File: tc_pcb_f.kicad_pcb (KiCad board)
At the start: 2 copper layers, 70 x 120 mm, 7 parts, among them U1 32u4, U2 MAX31855, U3 MAX31855, U4 MAX31855, U5 MAX31855, U6 MAX31855, U7 extPWR

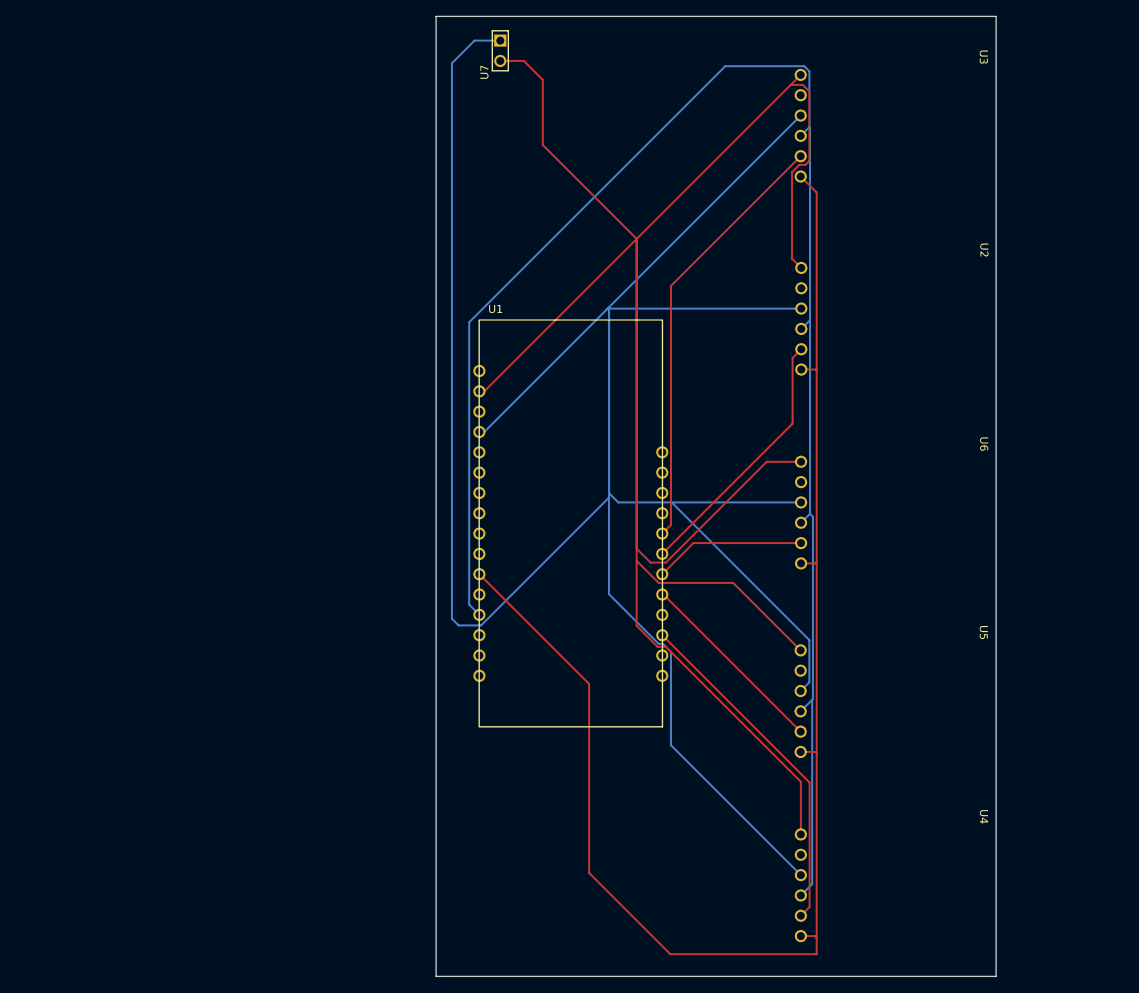
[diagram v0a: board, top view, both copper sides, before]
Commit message: finished layout for 8 sensor board
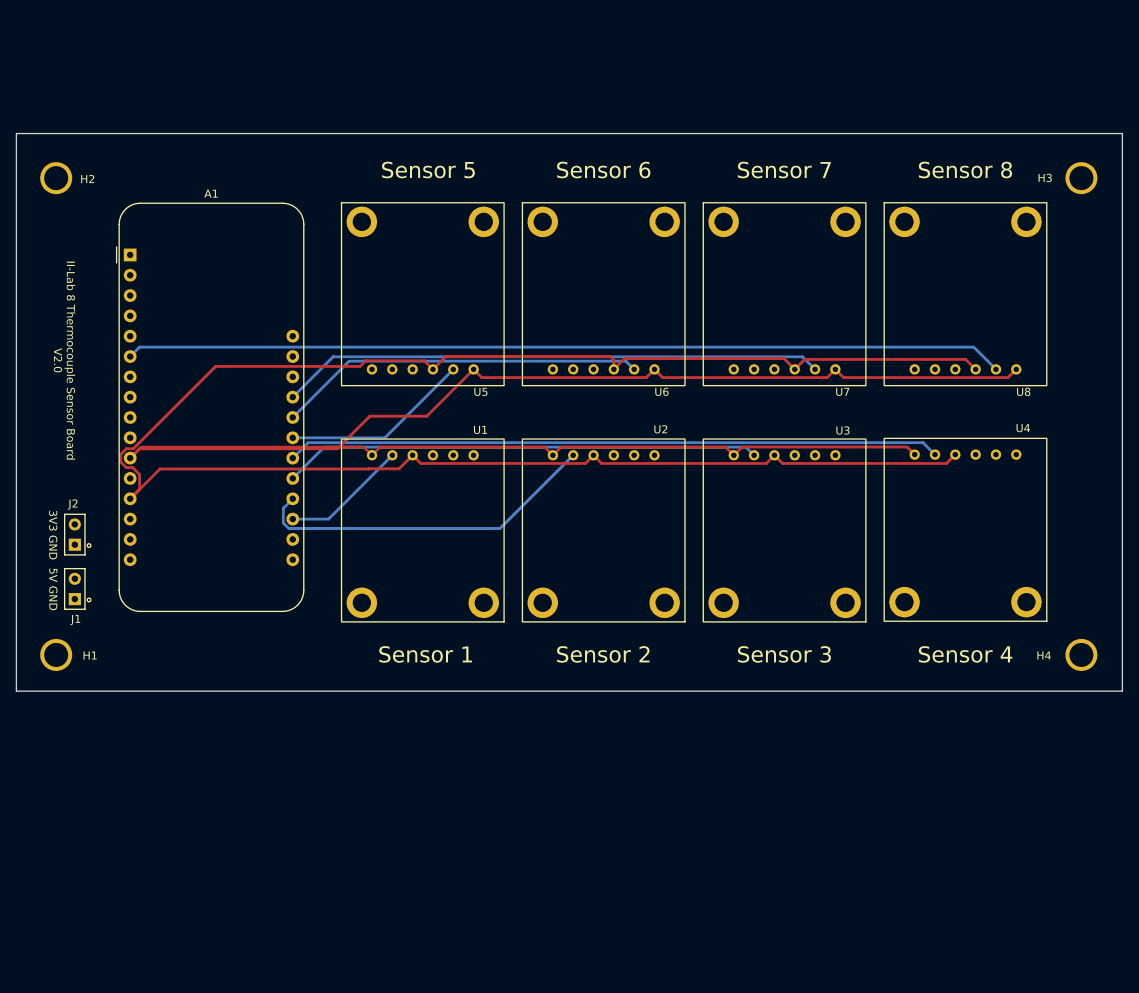
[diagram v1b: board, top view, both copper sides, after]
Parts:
- added A1: Adafruit_Feather_Generic, mcu:Adafruit_Feather, F.Cu at (61.8, 69.8)
- added H1: Conn_01x01, mounting_holes:3mm_hole, F.Cu at (58.9, 117.3)
- added H2: Conn_01x01, mounting_holes:3mm_hole, F.Cu at (52.9, 57.7)
- added H3: Conn_01x01, mounting_holes:3mm_hole, F.Cu at (181.1, 57.6)
- added H4: Conn_01x01, mounting_holes:3mm_hole, F.Cu at (69.0, 117.2)
- added J1: 5V Vin, dupont_connectors:dupont2x1, F.Cu at (52.3, 110.3)
- added J2: 3V3 Vin, dupont_connectors:dupont2x1, F.Cu at (52.3, 103.5)
- added U8: MAX31855, max:adafruit_max31855, F.Cu at (165.4, 78.4)
- U1: value 32u4 -> MAX31855; footprint thermo:32u4 -> max:adafruit_max31855
- U2, U3, U4, U5, U6: footprint thermo:MAX31855 -> max:adafruit_max31855
- U7: value extPWR -> MAX31855; footprint thermo:extPWR -> max:adafruit_max31855
- moved U5 74.5 mm to (97.6, 78.4), turned to 0 degrees
- moved U4 49.1 mm to (166.9, 100.5), turned to 180 degrees
- moved U7 48.7 mm to (142.8, 78.4), turned to 0 degrees
- moved U3 48.6 mm to (144.3, 100.5), turned to 180 degrees
- moved U6 42.4 mm to (120.2, 78.4), turned to 0 degrees
- moved U2 41.1 mm to (121.7, 100.5), turned to 180 degrees
- moved U1 18.0 mm to (99.1, 100.5), turned to 180 degrees
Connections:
- U1 pad 2: VCC -> +3V3
- U1 pad 3: unconnected-(U1-Pad3) -> GND
- U1 pad 4: GND -> MISO
- U1 pad 5: unconnected-(U1-Pad5) -> SS1
- U1 pad 6: unconnected-(U1-Pad6) -> SCK
- U2 pad 1: VCC -> unconnected-(U2-Pad1)
- U2 pad 2: unconnected-(U2-Pad2) -> +3V3
- U2 pad 4: PB3 -> MISO
- U2 pad 5: PB7 -> SS2
- U2 pad 6: PB1 -> SCK
- U3 pad 1: VCC -> unconnected-(U3-Pad1)
- U3 pad 2: unconnected-(U3-Pad2) -> +3V3
- U3 pad 4: PB3 -> MISO
- U3 pad 5: PD6 -> SS3
- U3 pad 6: PB1 -> SCK
- U4 pad 1: VCC -> unconnected-(U4-Pad1)
- U4 pad 2: unconnected-(U4-Pad2) -> +3V3
- U4 pad 4: PB3 -> MISO
- U4 pad 5: PC6 -> SS4
- U4 pad 6: PB1 -> SCK
- U5 pad 1: VCC -> unconnected-(U5-Pad1)
- U5 pad 2: unconnected-(U5-Pad2) -> +3V3
- U5 pad 4: PB3 -> MISO
- U5 pad 5: PB5 -> SS5
- U5 pad 6: PB1 -> SCK
- U6 pad 1: VCC -> unconnected-(U6-Pad1)
- U6 pad 2: unconnected-(U6-Pad2) -> +3V3
- U6 pad 4: PB3 -> MISO
- U6 pad 5: PB6 -> SS6
- U6 pad 6: PB1 -> SCK
- U7 pad 1: GND -> unconnected-(U7-Pad1)
- U7 pad 2: VCC -> +3V3
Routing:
- net GND: track 344.6 -> 0.00 mm
- net VCC: track 288.0 -> 0.00 mm
- net MISO: track 0.00 -> 231.8 mm
- net SCK: track 0.00 -> 219.5 mm
- net PB3: track 205.0 -> 0.00 mm
- net PB1: track 182.1 -> 0.00 mm
- net SS8: track 0.00 -> 109.9 mm
- net SS4: track 0.00 -> 81.7 mm
- net SS7: track 0.00 -> 68.0 mm
- net SS3: track 0.00 -> 59.7 mm
- net PD6: track 54.3 -> 0.00 mm
- net SS6: track 0.00 -> 46.0 mm
- net SS2: track 0.00 -> 43.8 mm
- net PC6: track 43.1 -> 0.00 mm
- net +5V: track 0.00 -> 41.5 mm
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- added copper zone on In2.Cu, net +3V3
- added copper zone on In1.Cu, net GND
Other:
- board size 70 x 120 mm -> 138.2 x 69.7 mm
- copper layers 2 -> 4
- board text added: "3V3 GND"
- board text added: "5V GND"
- board text added: "II-Lab 8 Thermocouple Sensor Board V2.0"
- board text added: "Sensor 1"
- board text added: "Sensor 2"
- board text added: "Sensor 3"
- board text added: "Sensor 4"
- board text added: "Sensor 5"
- board text added: "Sensor 6"
- board text added: "Sensor 7"
- board text added: "Sensor 8"

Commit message: commiting updates
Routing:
- net SCK: track 219.5 -> 220.3 mm
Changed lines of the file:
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@@
     (grid_origin 80.675 87.625)
     (pcbplotparams
-      (layerselection 0x00010f0_ffffffff)
+      (layerselection 0x00010fc_ffffffff)
       (disableapertmacros false)
       (usegerberextensions true)
@@
       (drillshape 0)
       (scaleselection 1)
-      (outputdirectory "GERBERS/")
+      (outputdirectory "gerbel/")
     )
   )
@@
   (segment (start 128.324511 85.147311) (end 148.887489 85.147311) (width 0.35) (layer "F.Cu") (net 8))
   (segment (start 91.725 89.975) (end 98.8358 89.975) (width 0.35) (layer "F.Cu") (net 8))
-  (segment (start 104.688 84.1228) (end 105.712511 85.147311) (width 0.35) (layer "F.Cu") (net 8))
   (segment (start 137.212 94.8604) (end 138.236511 93.835889) (width 0.35) (layer "F.Cu") (net 8))
   (segment (start 115.624511 93.835889) (end 136.187489 93.835889) (width 0.35) (layer "F.Cu") (net 8))
   (segment (start 113.575489 93.835889) (end 114.6 94.8604) (width 0.35) (layer "F.Cu") (net 8))
   (segment (start 150.936511 85.147311) (end 171.499489 85.147311) (width 0.35) (layer "F.Cu") (net 8))
-  (segment (start 105.712511 85.147311) (end 126.275489 85.147311) (width 0.35) (layer "F.Cu") (net 8))
+  (segment (start 105.712511 85.147311) (end 105.712511 85.187511) (width 0.35) (layer "F.Cu") (net 8))
+  (segment (start 104.688 84.1228) (end 105.712511 85.147311) (width 0.35) (layer "F.Cu") (net 8))
+  (segment (start 125.2728 86.15) (end 127.3 84.1228) (width 0.35) (layer "F.Cu") (net 8))
   (segment (start 127.3 84.1228) (end 128.324511 85.147311) (width 0.35) (layer "F.Cu") (net 8))
+  (segment (start 106.675 86.15) (end 125.2728 86.15) (width 0.35) (layer "F.Cu") (net 8))
   (segment (start 98.8358 89.975) (end 104.688 84.1228) (width 0.35) (layer "F.Cu") (net 8))
   (segment (start 158.882889 93.835889) (end 159.824 94.777) (width 0.35) (layer "F.Cu") (net 8))
   (segment (start 149.912 84.1228) (end 150.936511 85.147311) (width 0.35) (layer "F.Cu") (net 8))
   (segment (start 61.762 95.2166) (end 63.127489 93.851111) (width 0.35) (layer "F.Cu") (net 8))
+  (segment (start 105.712511 85.187511) (end 106.675 86.15) (width 0.35) (layer "F.Cu") (net 8))
   (segment (start 171.499489 85.147311) (end 172.524 84.1228) (width 0.35) (layer "F.Cu") (net 8))
   (segment (start 63.127489 93.851111) (end 90.978711 93.851111) (width 0.35) (layer "F.Cu") (net 8))
-  (segment (start 126.275489 85.147311) (end 127.3 84.1228) (width 0.35) (layer "F.Cu") (net 8))
   (segment (start 93.012511 93.835889) (end 113.575489 93.835889) (width 0.35) (layer "F.Cu") (net 8))
   (segment (start 136.187489 93.835889) (end 137.212 94.8604) (width 0.35) (layer "F.Cu") (net 8))
